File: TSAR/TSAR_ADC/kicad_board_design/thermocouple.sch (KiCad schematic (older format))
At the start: 2 parts, among them P1 CONN_02X13, P2 Phoenix 1984756 Terminal Block

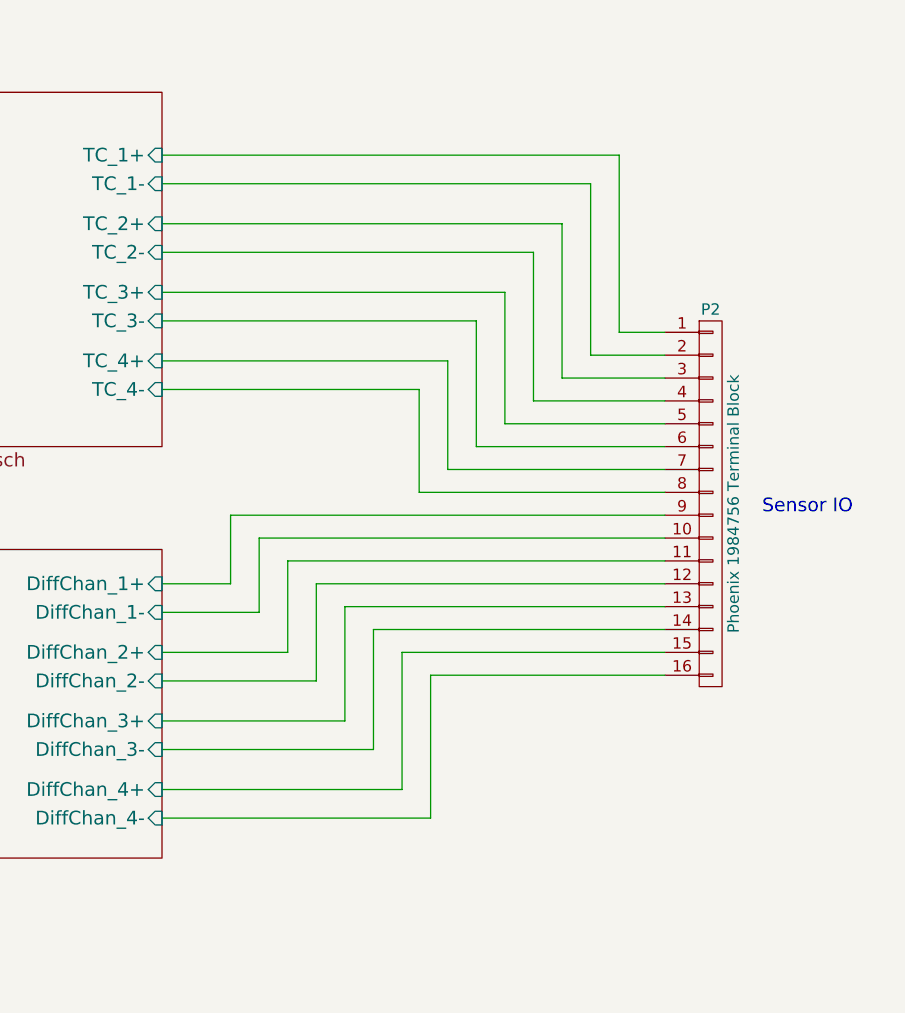
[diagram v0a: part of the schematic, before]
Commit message: Change from screw terminal block to DB-25.
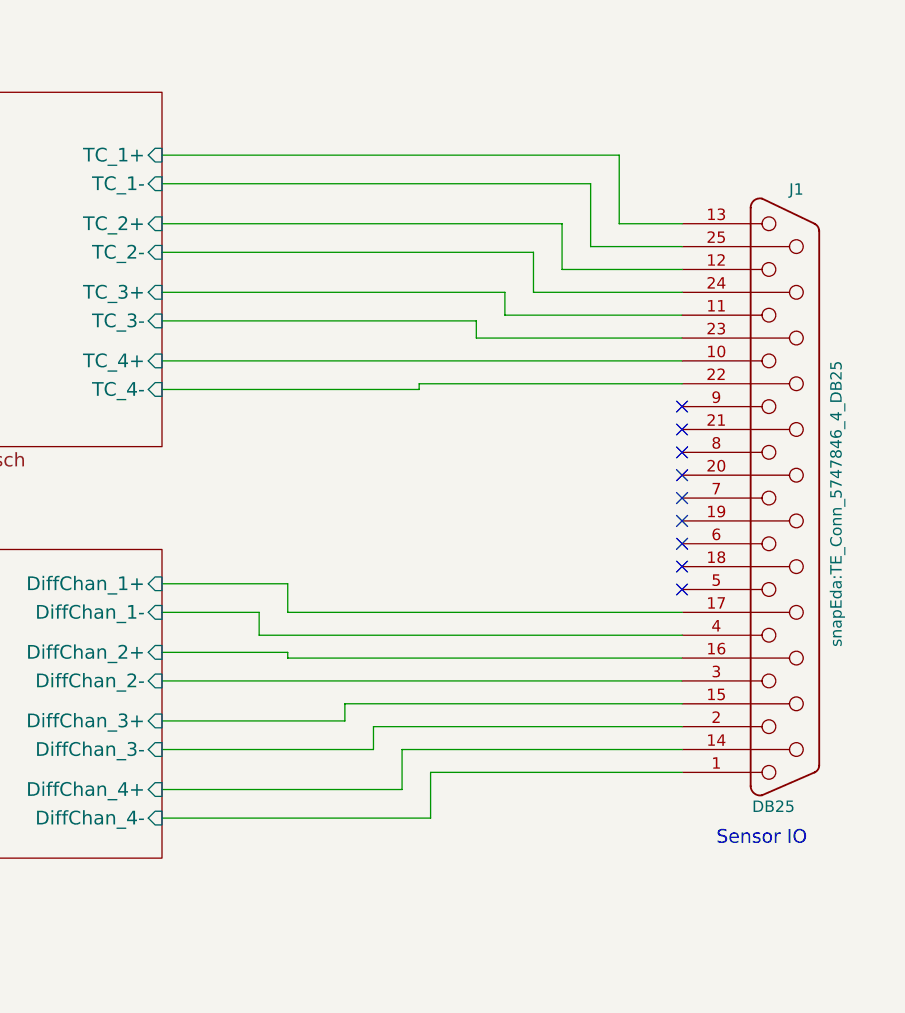
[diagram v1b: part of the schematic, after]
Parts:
- removed P2: Phoenix 1984756 Terminal Block, snapEda:1984756_phoenix_16_pos_terminal_block, symbol CONN_01X16
- added J1: DB25, snapEda:TE_Conn_5747846_4_DB25, symbol DB25
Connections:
- net pressure_ckt/DiffChan_1+: now also J1.17 (P17)
- net pressure_ckt/DiffChan_1-: now also J1.4
- net pressure_ckt/DiffChan_2+: now also J1.16 (P16)
- net pressure_ckt/DiffChan_2-: now also J1.3
- net pressure_ckt/DiffChan_3+: now also J1.15 (P15)
- net pressure_ckt/DiffChan_3-: now also J1.2
- net pressure_ckt/DiffChan_4+: now also J1.14 (P14)
- net pressure_ckt/DiffChan_4-: now also J1.1
- net thermocouple_ckt/TC_1+: now also J1.13
- net thermocouple_ckt/TC_1-: now also J1.25 (P25)
- net thermocouple_ckt/TC_2+: now also J1.12
- net thermocouple_ckt/TC_2-: now also J1.24 (P24)
- net thermocouple_ckt/TC_3+: now also J1.11
- net thermocouple_ckt/TC_3-: now also J1.23 (P23)
- net thermocouple_ckt/TC_4+: now also J1.10
- net thermocouple_ckt/TC_4-: now also J1.22 (P22)
- no-connect marks 18 -> 27

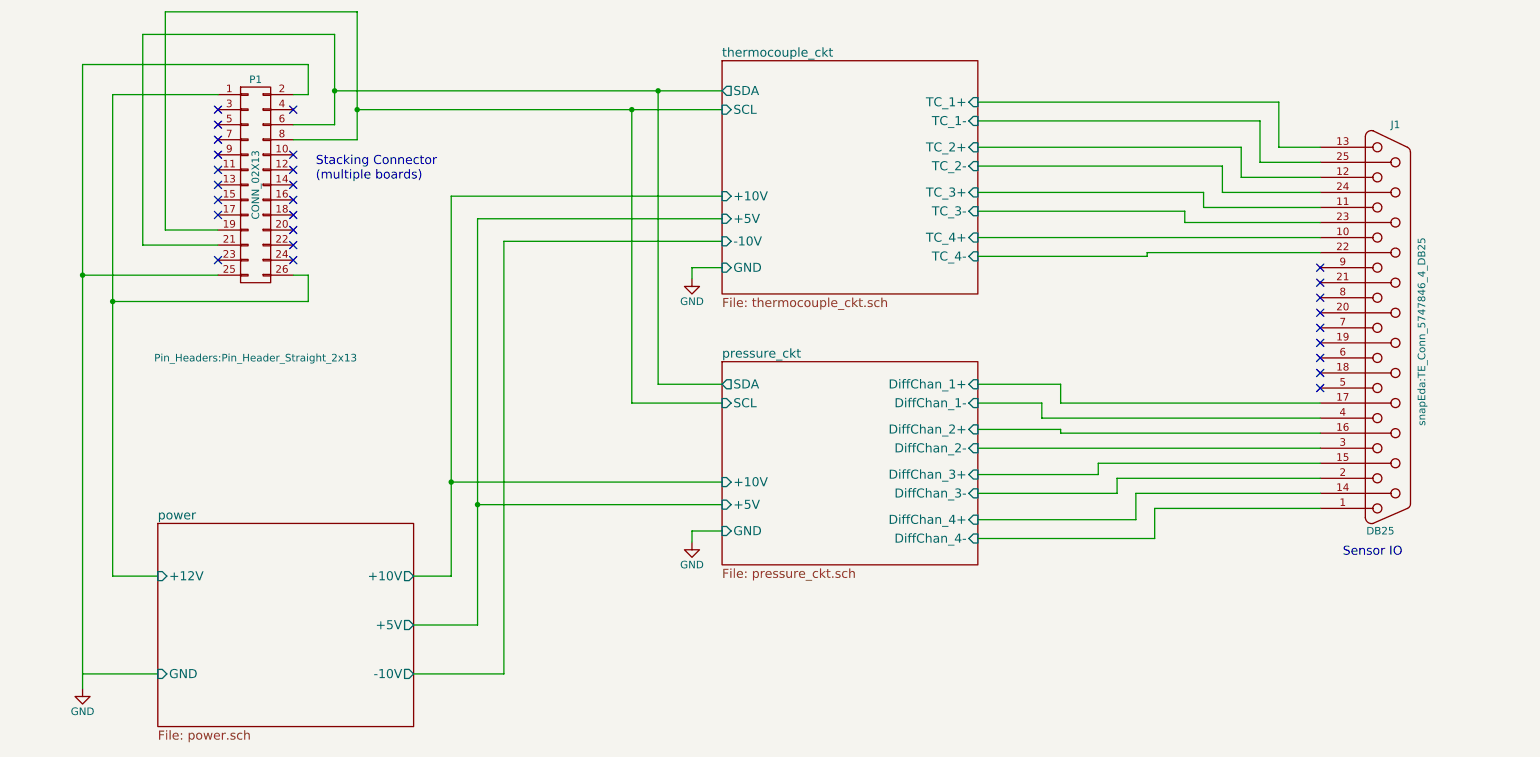
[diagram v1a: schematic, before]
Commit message: Simplify thermocouple signal chain for better worst case.
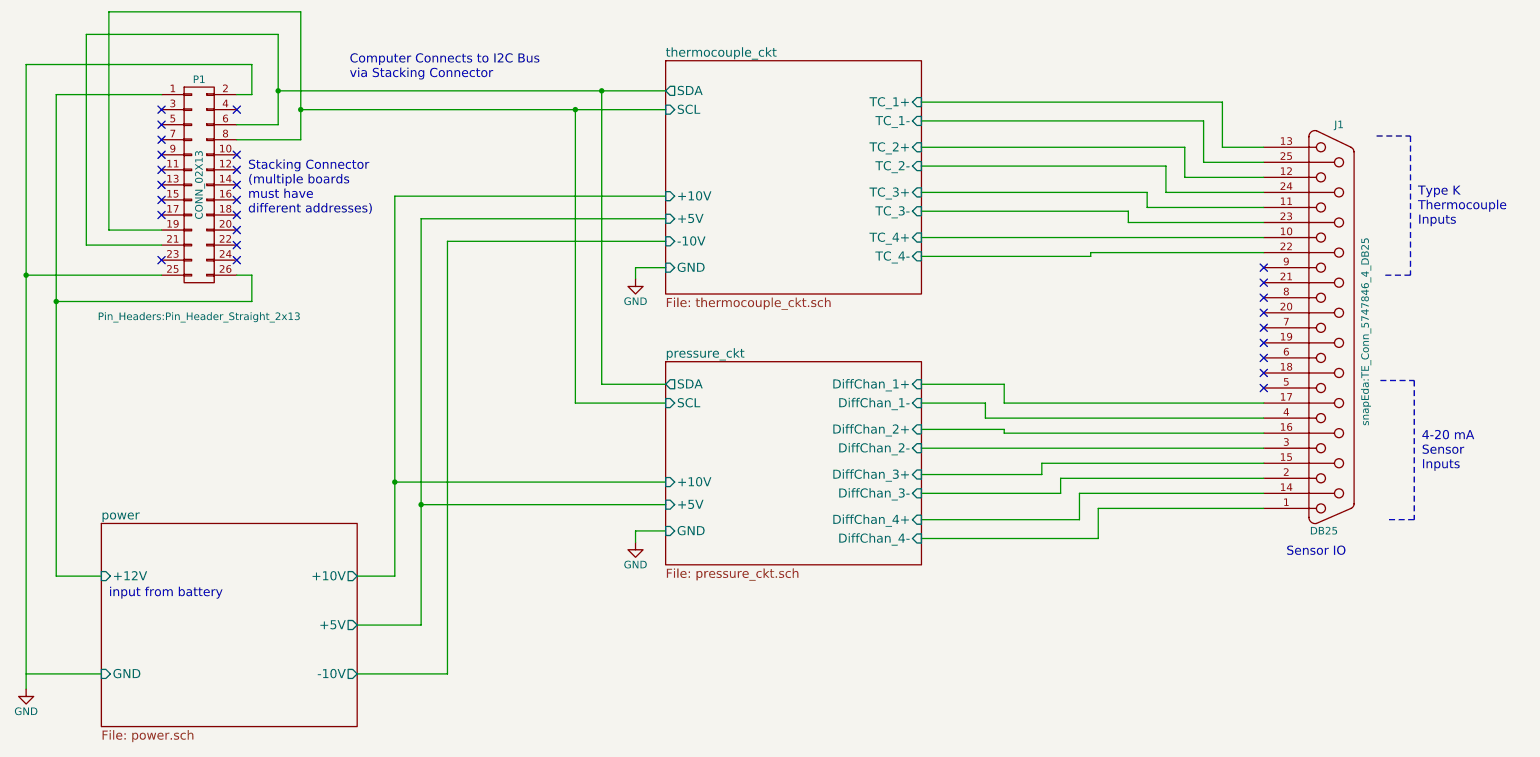
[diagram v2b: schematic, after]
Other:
- note added: "4-20 mA\nSensor \nInputs"
- note added: "Computer Connects to I2C Bus \nvia Stacking Connector"
- note added: "Stacking Connector\n(multiple boards\nmust have\ndifferent addresses)"
- note added: "Type K\nThermocouple\nInputs"
- note added: "input from battery"
- note removed: "Stacking Connector\n(multiple boards)"
- moved on the sheet: J1, P1

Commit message: Incorporate review comments.  Improve U1 routing, general schematic comments.
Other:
- note added: "input from battery\n(via stacking connector):\n12V nominal\nmin: 11.6V max: 27.6V"
- note removed: "input from battery"
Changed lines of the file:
@@
 NoConn ~ 9450 3400
 NoConn ~ 9450 4000
-Text Notes 1775 5400 0    60   ~ 0
-input from battery
+Text Notes 1525 4650 0    60   ~ 0
+input from battery\n(via stacking connector):\n12V nominal\nmin: 11.6V  max: 27.6V
 Text Notes 10475 2925 0    60   ~ 0
 Type K\nThermocouple\nInputs
